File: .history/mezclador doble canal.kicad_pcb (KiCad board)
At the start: 2 copper layers, 166 x 100.5 mm, 17 parts, among them J1 Conn_Coaxial, J2 Conn_Coaxial, J3 Conn_Coaxial, U1 NE5532

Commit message: completè el canal L
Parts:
- removed REF**: Jumper_Wire_10mm, personal:Jumper_Wire_10mm
- JP1: value Jumper_2_Bridged -> Jumper_2_Open; footprint Jumper:SolderJumper-2_P1.3mm_Bridged2Bar_Pad1.0x1.5mm -> personal:Jumper_Wire_10mm
- moved JP1 57.6 mm to (125.0, 77.0), turned to 180 degrees
- moved J2 38.1 mm to (137.7, 85.1), turned to -90 degrees
- moved RV2 31.1 mm to (112.0, 84.5)
- moved RV1 30.2 mm to (126.5, 69.8)
- moved J1 29.7 mm to (137.7, 101.6), turned to -90 degrees
- moved J3 27.8 mm to (108.0, 73.5), turned to 90 degrees
- moved C1 27.2 mm to (124.0, 83.0), turned to 90 degrees
- moved R6 21.4 mm to (118.8, 96.0)
- moved R1 20.8 mm to (128.6, 120.7), turned to 180 degrees
- moved C2 19.0 mm to (108.5, 95.2)
- moved C4 15.9 mm to (137.0, 119.2), turned to 90 degrees
- moved R9 14.4 mm to (128.8, 88.9), turned to 180 degrees
- moved R10 14.0 mm to (118.8, 103.5)
- moved R2 13.2 mm to (113.8, 106.0), turned to 180 degrees
- moved C3 8.28 mm to (125.0, 110.0), turned to -90 degrees
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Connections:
- C1 pad 2: Net-(C1-Pad2) -> Net-(JP1-B)
- JP1 pad 1: unconnected-(JP1-A-Pad1) -> Net-(JP1-A)
- JP1 pad 2: unconnected-(JP1-B-Pad2) -> Net-(JP1-B)
- RV1 pad 2: Net-(C1-Pad2) -> Net-(JP1-A)
- U1 pad 4: unconnected-(U1C-V--Pad4) -> GND
- U1 pad 8: unconnected-(U1C-V+-Pad8) -> VCC
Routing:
- net GND: track 0.00 -> 106.8 mm
- net Net-(U1A--): track 0.00 -> 45.9 mm
- net Net-(C3-Pad2): track 0.00 -> 39.7 mm
- net Net-(U1A-+): track 0.00 -> 25.4 mm
- net Net-(J2-In): track 0.00 -> 20.3 mm
- net Net-(J1-In): track 0.00 -> 18.4 mm
- net VCC: track 0.00 -> 17.2 mm
- net Net-(J3-In): track 0.00 -> 12.7 mm
- net Net-(C2-Pad2): track 0.00 -> 11.3 mm
- net Net-(C2-Pad1): track 0.00 -> 11.0 mm
- net Net-(JP1-A): track 0.00 -> 9.65 mm
- net Net-(C1-Pad1): track 0.00 -> 8.12 mm
- net Net-(JP1-B): track 0.00 -> 5.45 mm
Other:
- board size 166 x 100.5 mm -> 44.5 x 63.5 mm

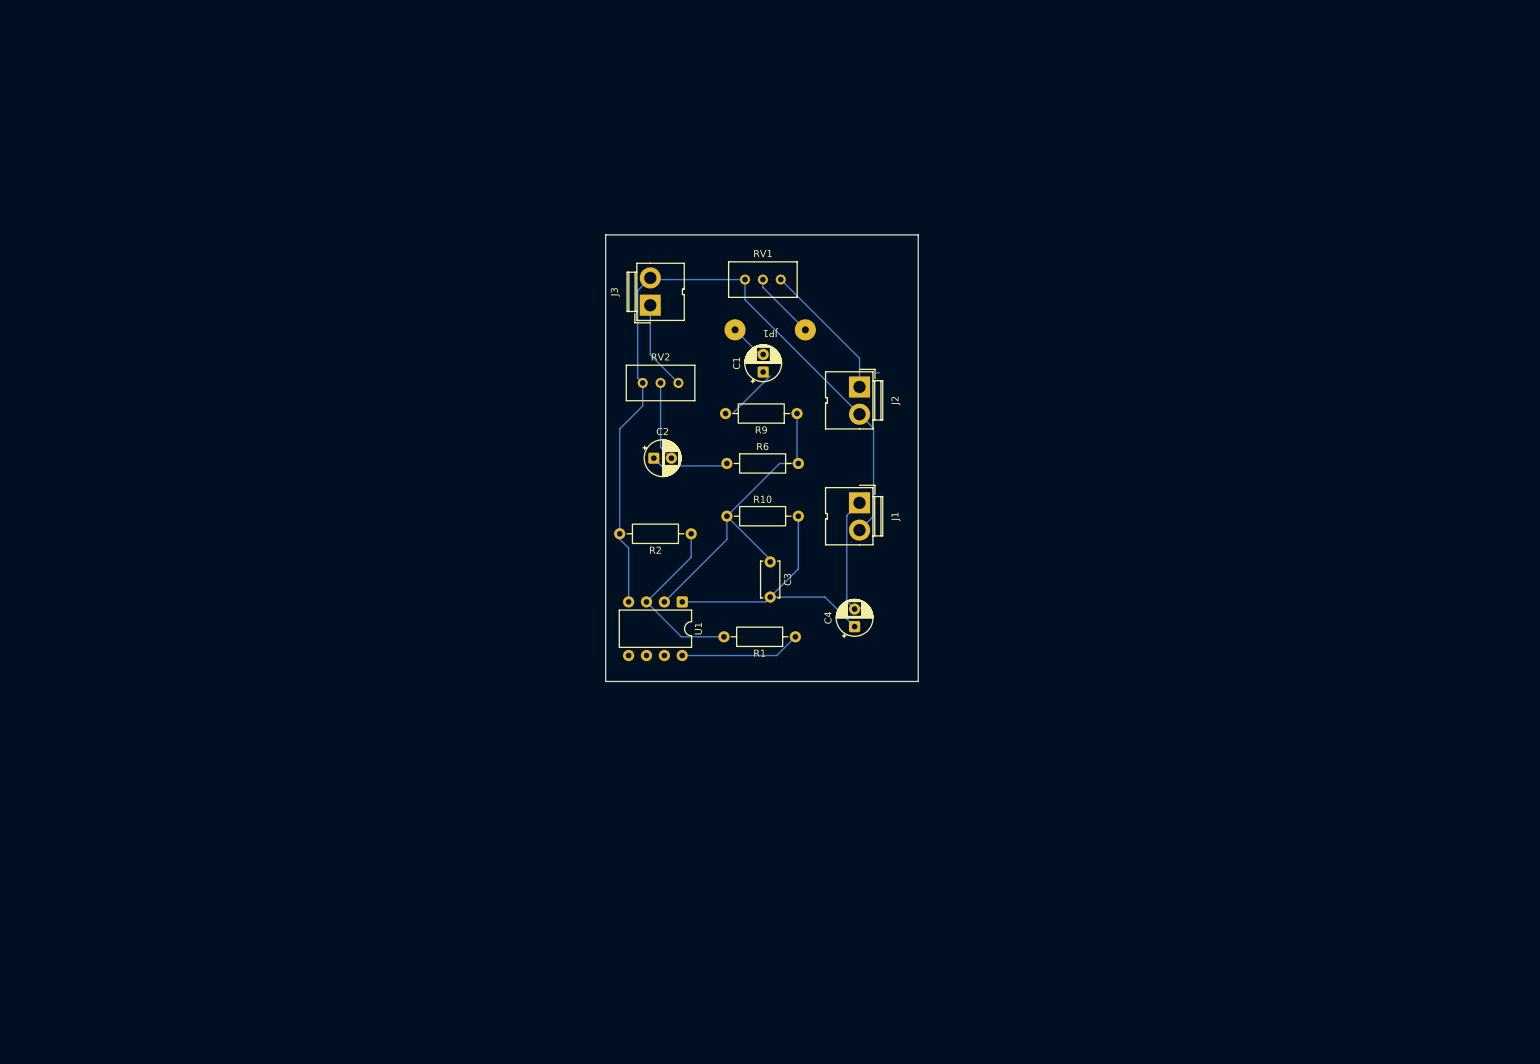
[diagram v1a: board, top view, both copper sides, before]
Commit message: agregando canal r
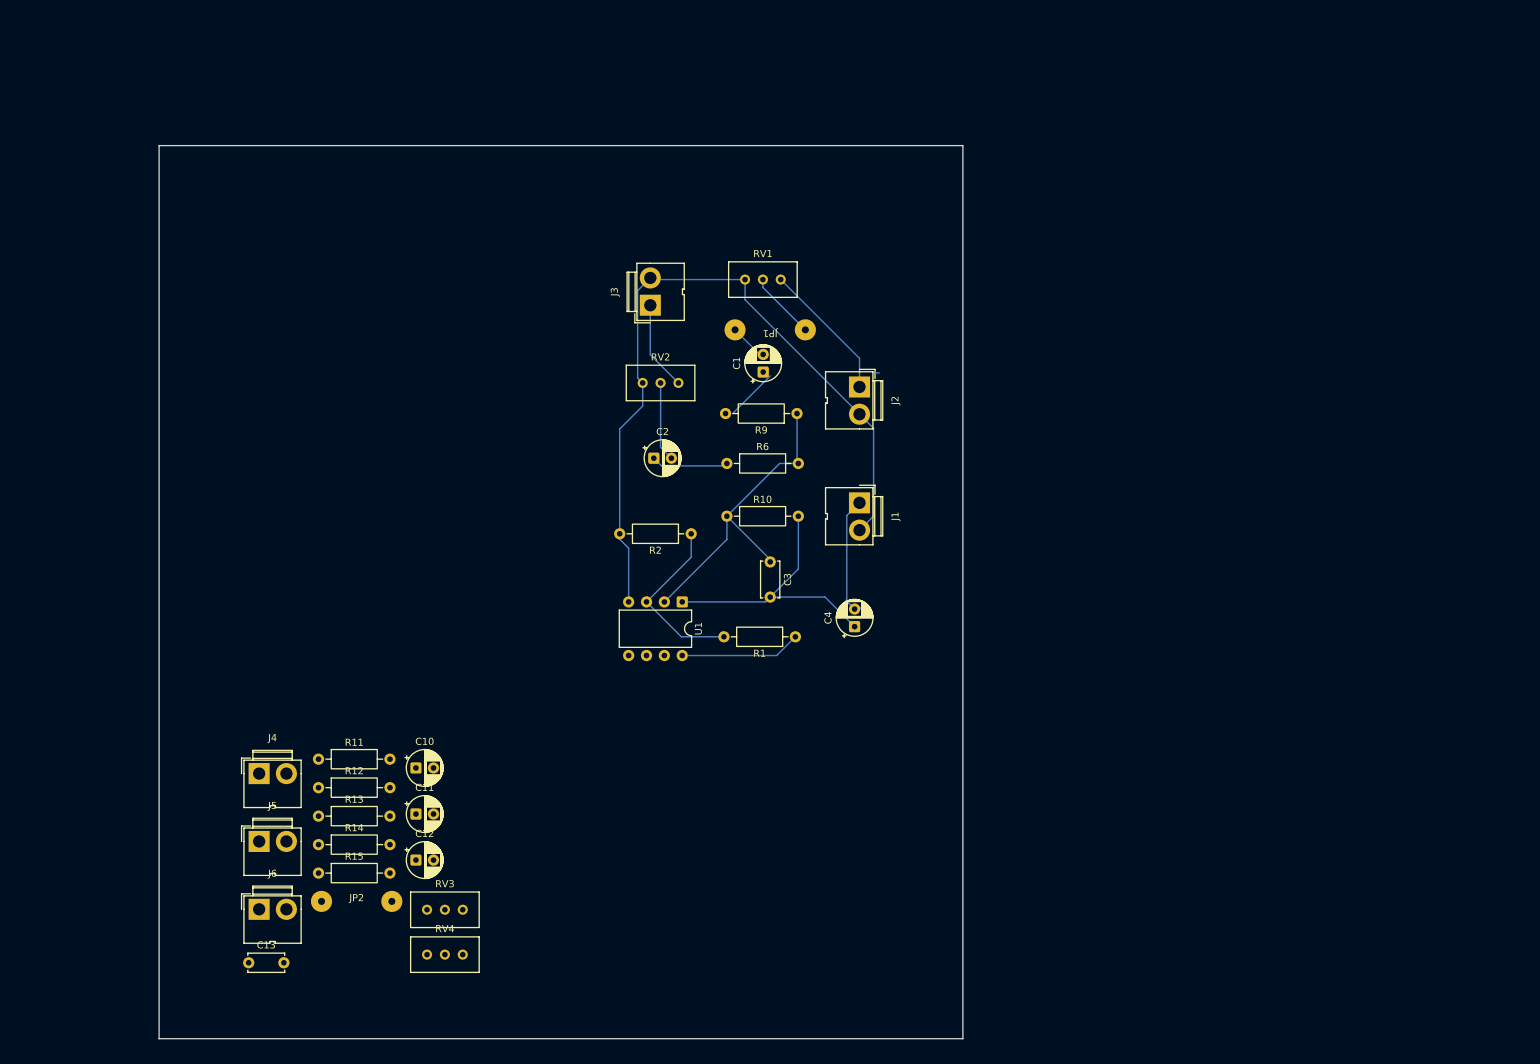
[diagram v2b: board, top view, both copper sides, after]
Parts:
- added C10: C_Polarized_US, Capacitor_THT:CP_Radial_D5.0mm_P2.50mm, F.Cu at (74.6, 139.3)
- added C11: C_Polarized_US, Capacitor_THT:CP_Radial_D5.0mm_P2.50mm, F.Cu at (74.6, 145.8)
- added C12: C_Polarized, Capacitor_THT:CP_Radial_D5.0mm_P2.50mm, F.Cu at (74.6, 152.4)
- added C13: C, Capacitor_THT:C_Disc_D5.0mm_W2.5mm_P5.00mm, F.Cu at (50.8, 167.0)
- added J4: Conn_Coaxial, Connector:JWT_A3963_1x02_P3.96mm_Vertical, F.Cu at (52.3, 140.1)
- added J5: Conn_Coaxial, Connector:JWT_A3963_1x02_P3.96mm_Vertical, F.Cu at (52.3, 149.8)
- added J6: Conn_Coaxial, Connector:JWT_A3963_1x02_P3.96mm_Vertical, F.Cu at (52.3, 159.4)
- added JP2: Jumper_2_Open, personal:Jumper_Wire_10mm, F.Cu at (66.2, 158.3)
- added R11: R, Resistor_THT:R_Axial_DIN0207_L6.3mm_D2.5mm_P10.16mm_Horizontal, F.Cu at (60.8, 138.1)
- added R12: R, Resistor_THT:R_Axial_DIN0207_L6.3mm_D2.5mm_P10.16mm_Horizontal, F.Cu at (60.8, 142.1)
- added R13: R, Resistor_THT:R_Axial_DIN0207_L6.3mm_D2.5mm_P10.16mm_Horizontal, F.Cu at (60.8, 146.2)
- added R14: R, Resistor_THT:R_Axial_DIN0207_L6.3mm_D2.5mm_P10.16mm_Horizontal, F.Cu at (60.8, 150.2)
- added R15: R, Resistor_THT:R_Axial_DIN0207_L6.3mm_D2.5mm_P10.16mm_Horizontal, F.Cu at (60.8, 154.2)
- added RV3: R_Potentiometer, Potentiometer_THT:Potentiometer_Bourns_3296W_Vertical, F.Cu at (81.3, 159.5)
- added RV4: R_Potentiometer, Potentiometer_THT:Potentiometer_Bourns_3296W_Vertical, F.Cu at (81.3, 165.8)
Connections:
- RV2 pad 1: Net-(J3-In) -> GND
- RV2 pad 3: GND -> Net-(J3-In)
- U1 pad 5: unconnected-(U1B-+-Pad5) -> Net-(U1B-+)
- U1 pad 6: unconnected-(U1B---Pad6) -> Net-(U1B--)
- U1 pad 7: unconnected-(U1-Pad7) -> Net-(C12-Pad1)
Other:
- board size 44.5 x 63.5 mm -> 114.3 x 127 mm

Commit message: separando componentes
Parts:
- moved J4 38.5 mm to (50.8, 101.6)
- moved R11 29.8 mm to (78.7, 114.3)
- moved J5 22.8 mm to (50.8, 127.0)
- moved RV3 21.5 mm to (101.6, 152.4)
- moved RV4 20.3 mm to (101.6, 165.1)
- moved C10 17.0 mm to (86.4, 127.0)
- moved J6 7.16 mm to (50.8, 152.4)
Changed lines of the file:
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@@
 	(footprint "Potentiometer_THT:Potentiometer_Bourns_3296W_Vertical"
 		(layer "F.Cu")
-		(at 81.28 159.46)
+		(at 101.6 152.4)
 		(descr "Potentiometer, vertical, Bourns 3296W, https://www.bourns.com/pdfs/3296.pdf")
 		(tags "Potentiometer vertical Bourns 3296W")
@@
 	(footprint "Potentiometer_THT:Potentiometer_Bourns_3296W_Vertical"
 		(layer "F.Cu")
-		(at 81.28 165.84)
+		(at 101.6 165.1)
 		(descr "Potentiometer, vertical, Bourns 3296W, https://www.bourns.com/pdfs/3296.pdf")
 		(tags "Potentiometer vertical Bourns 3296W")
@@
 	(footprint "Resistor_THT:R_Axial_DIN0207_L6.3mm_D2.5mm_P10.16mm_Horizontal"
 		(layer "F.Cu")
-		(at 60.77 138.05)
+		(at 78.74 114.3)
 		(descr "Resistor, Axial_DIN0207 series, Axial, Horizontal, pin pitch=10.16mm, 0.25W = 1/4W, length*diameter=6.3*2.5mm^2, http://cdn-reichelt.de/documents/datenblatt/B400/1_4W%23YAG.pdf")
 		(tags "Resistor Axial_DIN0207 series Axial Horizontal pin pitch 10.16mm 0.25W = 1/4W length 6.3mm diameter 2.5mm")
@@
 	(footprint "Connector:JWT_A3963_1x02_P3.96mm_Vertical"
 		(layer "F.Cu")
-		(at 52.325 159.4)
+		(at 50.8 152.4)
 		(descr "JWT A3963, 3.96mm pitch Pin head connector (http://www.jwt.com.tw/pro_pdf/A3963.pdf)")
 		(tags "connector JWT A3963 pinhead")
@@
 	(footprint "Connector:JWT_A3963_1x02_P3.96mm_Vertical"
 		(layer "F.Cu")
-		(at 52.325 140.1)
+		(at 50.8 101.6)
 		(descr "JWT A3963, 3.96mm pitch Pin head connector (http://www.jwt.com.tw/pro_pdf/A3963.pdf)")
 		(tags "connector JWT A3963 pinhead")
@@
 	(footprint "Capacitor_THT:CP_Radial_D5.0mm_P2.50mm"
 		(layer "F.Cu")
-		(at 74.619775 139.3)
+		(at 86.4 127)
 		(descr "CP, Radial series, Radial, pin pitch=2.50mm, diameter=5mm, height=7mm, Electrolytic Capacitor")
 		(tags "CP Radial series Radial pin pitch 2.50mm diameter 5mm height 7mm Electrolytic Capacitor")
@@
 	(footprint "Connector:JWT_A3963_1x02_P3.96mm_Vertical"
 		(layer "F.Cu")
-		(at 52.325 149.75)
+		(at 50.8 127)
 		(descr "JWT A3963, 3.96mm pitch Pin head connector (http://www.jwt.com.tw/pro_pdf/A3963.pdf)")
 		(tags "connector JWT A3963 pinhead")
@@
 	)
 	(segment
-		(start 123.96 70.96)
-		(end 130 77)
+		(start 103.6 106.78)
+		(end 104.87 108.05)
 		(width 0.2)
 		(layer "B.Cu")
-		(net "Net-(JP1-A)")
+		(net "GND")
 	)
 	(segment
-		(start 123.96 69.85)
-		(end 123.96 70.96)
+		(start 106.150001 83.830001)
+		(end 106.87 84.55)
 		(width 0.2)
 		(layer "B.Cu")
-		(net "Net-(JP1-A)")
+		(net "GND")
 	)
 	(segment
-		(start 123.5 80.5)
-		(end 124 80.5)
+		(start 121.42 72.72)
+		(end 137.7 89)
 		(width 0.2)
 		(layer "B.Cu")
-		(net "Net-(JP1-B)")
+		(net "GND")
 	)
 	(segment
-		(start 120 77)
-		(end 123.5 80.5)
+		(start 121.42 69.85)
+		(end 121.42 72.72)
 		(width 0.2)
 		(layer "B.Cu")
-		(net "Net-(JP1-B)")
+		(net "GND")
 	)
 	(segment
-		(start 129 111)
-		(end 125 115)
+		(start 106.87 87.82)
+		(end 103.6 91.09)
 		(width 0.2)
 		(layer "B.Cu")
-		(net "Net-(C3-Pad2)")
+		(net "GND")
 	)
 	(segment
-		(start 112.49 115.69)
-		(end 124.31 115.69)
+		(start 107.95 69.62)
+		(end 108.18 69.85)
 		(width 0.2)
 		(layer "B.Cu")
-		(net "Net-(C3-Pad2)")
+		(net "GND")
 	)
 	(segment
-		(start 129 103.5)
-		(end 129 111)
+		(start 104.87 108.05)
+		(end 104.87 115.69)
 		(width 0.2)
 		(layer "B.Cu")
-		(net "Net-(C3-Pad2)")
+		(net "GND")
 	)
 	(segment
-		(start 125 115)
-		(end 132.794887 115)
+		(start 137.7 89)
+		(end 139.7 91)
 		(width 0.2)
 		(layer "B.Cu")
-		(net "Net-(C3-Pad2)")
+		(net "GND")
 	)
 	(segment
-		(start 132.794887 115)
-		(end 137 119.205113)
+		(start 139.7 103.48)
+		(end 137.7 105.48)
 		(width 0.2)
 		(layer "B.Cu")
-		(net "Net-(C3-Pad2)")
+		(net "GND")
 	)
 	(segment
-		(start 124.31 115.69)
-		(end 125 115)
+		(start 106.15 71.42)
+		(end 106.150001 83.830001)
 		(width 0.2)
 		(layer "B.Cu")
-		(net "Net-(C3-Pad2)")
+		(net "GND")
 	)
 	(segment
-		(start 135.9 115.605113)
-		(end 137 116.705113)
+		(start 106.87 84.55)
+		(end 106.87 87.82)
 		(width 0.2)
 		(layer "B.Cu")
-		(net "Net-(J1-In)")
+		(net "GND")
 	)
 	(segment
-		(start 137.75 116.455113)
-		(end 138 116.705113)
+		(start 121.3 69.62)
+		(end 121.42 69.5)
 		(width 0.2)
 		(layer "B.Cu")
-		(net "Net-(J1-In)")
+		(net "GND")
 	)
 	(segment
-		(start 135.9 103.4)
-		(end 135.9 115.605113)
+		(start 108.18 69.85)
+		(end 121.42 69.85)
 		(width 0.2)
 		(layer "B.Cu")
-		(net "Net-(J1-In)")
+		(net "GND")
 	)
 	(segment
-		(start 135.75 115.455113)
-		(end 137 116.705113)
+		(start 103.6 91.09)
+		(end 103.6 106)
 		(width 0.2)
 		(layer "B.Cu")
-		(net "Net-(J1-In)")
+		(net "GND")
 	)
 	(segment
-		(start 137.7 101.6)
-		(end 135.9 103.4)
+		(start 103.6 106)
+		(end 103.6 106.78)
 		(width 0.2)
 		(layer "B.Cu")
-		(net "Net-(J1-In)")
+		(net "GND")
 	)
 	(segment
-		(start 126.5 69.85)
-		(end 137.7 81.05)
+		(start 139.7 91)
+		(end 139.7 103.48)
 		(width 0.2)
 		(layer "B.Cu")
-		(net "Net-(J2-In)")
+		(net "GND")
 	)
 	(segment
-		(start 140.12 83.12)
-		(end 140.5 83.12)
+		(start 107.95 69.62)
+		(end 106.15 71.42)
 		(width 0.2)
 		(layer "B.Cu")
-		(net "Net-(J2-In)")
+		(net "GND")
 	)
 	(segment
-		(start 137.7 81.05)
-		(end 137.7 85.12)
+		(start 123.96 70.96)
+		(end 130 77)
 		(width 0.2)
 		(layer "B.Cu")
-		(net "Net-(J2-In)")
+		(net "Net-(JP1-A)")
 	)
 	(segment
-		(start 103.6 106.78)
-		(end 104.87 108.05)
+		(start 123.96 69.85)
+		(end 123.96 70.96)
 		(width 0.2)
 		(layer "B.Cu")
-		(net "GND")
+		(net "Net-(JP1-A)")
 	)
 	(segment
-		(start 106.150001 83.830001)
-		(end 106.87 84.55)
+		(start 123.5 80.5)
+		(end 124 80.5)
 		(width 0.2)
 		(layer "B.Cu")
-		(net "GND")
+		(net "Net-(JP1-B)")
 	)
 	(segment
-		(start 121.42 72.72)
-		(end 137.7 89)
+		(start 120 77)
+		(end 123.5 80.5)
 		(width 0.2)
 		(layer "B.Cu")
-		(net "GND")
+		(net "Net-(JP1-B)")
 	)
 	(segment
-		(start 121.42 69.85)
-		(end 121.42 72.72)
+		(start 129 111)
+		(end 125 115)
 		(width 0.2)
 		(layer "B.Cu")
-		(net "GND")
+		(net "Net-(C3-Pad2)")
 	)
 	(segment
-		(start 106.87 87.82)
-		(end 103.6 91.09)
+		(start 112.49 115.69)
+		(end 124.31 115.69)
 		(width 0.2)
 		(layer "B.Cu")
-		(net "GND")
+		(net "Net-(C3-Pad2)")
 	)
 	(segment
-		(start 107.95 69.62)
-		(end 108.18 69.85)
+		(start 129 103.5)
+		(end 129 111)
 		(width 0.2)
 		(layer "B.Cu")
-		(net "GND")
+		(net "Net-(C3-Pad2)")
 	)
 	(segment
-		(start 104.87 108.05)
-		(end 104.87 115.69)
+		(start 125 115)
+		(end 132.794887 115)
 		(width 0.2)
 		(layer "B.Cu")
-		(net "GND")
+		(net "Net-(C3-Pad2)")
 	)
 	(segment
-		(start 137.7 89)
-		(end 139.7 91)
+		(start 132.794887 115)
+		(end 137 119.205113)
 		(width 0.2)
 		(layer "B.Cu")
-		(net "GND")
+		(net "Net-(C3-Pad2)")
 	)
 	(segment
-		(start 139.7 103.48)
-		(end 137.7 105.48)
+		(start 124.31 115.69)
+		(end 125 115)
 		(width 0.2)
 		(layer "B.Cu")
-		(net "GND")
+		(net "Net-(C3-Pad2)")
 	)
 	(segment
-		(start 106.15 71.42)
-		(end 106.150001 83.830001)
+		(start 135.9 115.605113)
+		(end 137 116.705113)
 		(width 0.2)
 		(layer "B.Cu")
-		(net "GND")
+		(net "Net-(J1-In)")
 	)
 	(segment
-		(start 106.87 84.55)
-		(end 106.87 87.82)
+		(start 137.75 116.455113)
+		(end 138 116.705113)
 		(width 0.2)
 		(layer "B.Cu")
-		(net "GND")
+		(net "Net-(J1-In)")
 	)
 	(segment
-		(start 121.3 69.62)
-		(end 121.42 69.5)
+		(start 135.9 103.4)
+		(end 135.9 115.605113)
 		(width 0.2)
 		(layer "B.Cu")
-		(net "GND")
+		(net "Net-(J1-In)")
 	)
 	(segment
-		(start 108.18 69.85)
-		(end 121.42 69.85)
+		(start 135.75 115.455113)
+		(end 137 116.705113)
 		(width 0.2)
 		(layer "B.Cu")
-		(net "GND")
+		(net "Net-(J1-In)")
 	)
 	(segment
-		(start 103.6 91.09)
-		(end 103.6 106)
+		(start 137.7 101.6)
+		(end 135.9 103.4)
 		(width 0.2)
 		(layer "B.Cu")
-		(net "GND")
+		(net "Net-(J1-In)")
 	)
 	(segment
-		(start 103.6 106)
-		(end 103.6 106.78)
+		(start 125.92 123.31)
+		(end 112.49 123.31)
 		(width 0.2)
 		(layer "B.Cu")
-		(net "GND")
+		(net "VCC")
 	)
 	(segment
-		(start 139.7 91)
-		(end 139.7 103.48)
+		(start 128.58 120.65)
+		(end 125.92 123.31)
 		(width 0.2)
 		(layer "B.Cu")
-		(net "GND")
+		(net "VCC")
 	)
 	(segment
-		(start 107.95 69.62)
-		(end 106.15 71.42)
+		(start 126.5 69.85)
+		(end 137.7 81.05)
 		(width 0.2)
 		(layer "B.Cu")
-		(net "GND")
+		(net "Net-(J2-In)")
+	)
+	(segment
+		(start 140.12 83.12)
+		(end 140.5 83.12)
+		(width 0.2)
+		(layer "B.Cu")
+		(net "Net-(J2-In)")
+	)
+	(segment
+		(start 137.7 81.05)
+		(end 137.7 85.12)
+		(width 0.2)
+		(layer "B.Cu")
+		(net "Net-(J2-In)")
 	)
 	(segment
@@
 	)
 	(segment
-		(start 125.92 123.31)
-		(end 112.49 123.31)
-		(width 0.2)
-		(layer "B.Cu")
-		(net "VCC")
-	)
-	(segment
-		(start 128.58 120.65)
-		(end 125.92 123.31)
-		(width 0.2)
-		(layer "B.Cu")
-		(net "VCC")
-	)
-	(segment

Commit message: trabajando canal R
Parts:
- removed JP2: Jumper_2_Open, personal:Jumper_Wire_10mm
- added J7: Screw_Terminal_01x02, Connector:JWT_A3963_1x02_P3.96mm_Vertical, F.Cu at (177.8, 40.8)
- moved J5 161.0 mm to (186.8, 40.8), turned to 90 degrees
- moved C13 158.3 mm to (195.2, 102.0)
- moved R14 152.2 mm to (203.2, 96.6), turned to 180 degrees
- moved R15 140.3 mm to (193.0, 107.4)
- moved R11 114.6 mm to (186.8, 76.2), turned to 90 degrees
- moved J1 93.8 mm to (225.8, 69.3)
- moved J2 93.8 mm to (225.8, 52.8)
- moved C2 93.8 mm to (196.6, 62.9)
- moved J3 93.8 mm to (196.1, 41.2)
- moved R2 93.8 mm to (201.9, 73.7)
- moved RV2 93.8 mm to (200.1, 52.2)
- moved U1 93.8 mm to (200.6, 83.4)
- moved C1 93.8 mm to (212.1, 50.7)
- moved C3 93.8 mm to (213.1, 77.7)
- moved C4 93.8 mm to (225.1, 86.9)
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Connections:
- C10 pad 2: Net-(JP2-B) -> Net-(C10-Pad2)
- RV3 pad 2: Net-(JP2-A) -> Net-(C10-Pad2)
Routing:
- net GND: track 106.8 -> 125.2 mm
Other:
- board size 114.3 x 127 mm -> 60.4 x 124 mm
- board text added: "nestorotero@abc.gob.ar"

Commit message: reduciendo espacio desperdiciado
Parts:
- moved C12 182.8 mm to (188.2, 99.6)
- moved C11 153.7 mm to (177.1, 68.5), turned to -90 degrees
- moved J4 140.7 mm to (177.8, 102.5), turned to 90 degrees
- moved R13 140.2 mm to (176.6, 65.0), turned to 90 degrees
- moved J6 119.8 mm to (179.4, 86.9), turned to -90 degrees
- moved R12 117.8 mm to (183.1, 62.7), turned to -90 degrees
- moved RV4 114.0 mm to (181.6, 77.2), turned to 0 degrees
- moved C10 105.3 mm to (181.7, 56.8)
- moved RV3 92.7 mm to (189.4, 58.5), turned to 180 degrees
- moved RV2 15.5 mm to (193.9, 66.5), turned to 180 degrees
- moved C1 11.5 mm to (211.9, 62.2)
- moved JP1 10.4 mm to (211.8, 55.0)
- moved R9 10.4 mm to (216.7, 67.0)
- moved C2 10.2 mm to (198.0, 73.0), turned to 180 degrees
- moved J7 9.79 mm to (176.5, 50.5)
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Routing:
- net VCC: track 17.2 -> 131.6 mm
- net Net-(U1B--): track 0.00 -> 33.8 mm
- net Net-(C12-Pad1): track 0.00 -> 29.6 mm
- net Net-(U1B-+): track 0.00 -> 13.8 mm
- net Net-(J4-In): track 0.00 -> 12.6 mm
- net Net-(J6-In): track 0.00 -> 10.9 mm
- net Net-(C10-Pad2): track 0.00 -> 9.30 mm
- net Net-(J5-In): track 0.00 -> 9.00 mm
- net Net-(C11-Pad2): track 0.00 -> 6.98 mm
- net Net-(C10-Pad1): track 0.00 -> 6.47 mm
- net Net-(U1A--): track 45.9 -> 39.5 mm
- net Net-(J1-In): track 18.4 -> 13.3 mm
- net Net-(C2-Pad2): track 11.3 -> 6.90 mm
- net Net-(J3-In): track 12.7 -> 17.0 mm
- net Net-(U1A-+): track 25.4 -> 21.2 mm
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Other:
- board size 60.4 x 124 mm -> 56.7 x 63.9 mm

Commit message: acomodando componentes
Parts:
- moved C4 16.8 mm to (222.2, 70.3)
- moved R1 15.5 mm to (225.6, 75.7)
- moved J2 14.3 mm to (223.7, 47.8)
- moved J1 13.5 mm to (224.5, 61.5)
- moved C3 6.56 mm to (206.5, 75.8), turned to 0 degrees
- moved R6 5.07 mm to (206.4, 66.5)
- moved R10 4.94 mm to (206.5, 71.4)
- moved R9 4.62 mm to (216.5, 62.3)
- moved C1 4.00 mm to (211.9, 58.2)
- moved JP1 2.00 mm to (211.8, 53.0)
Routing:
- net GND: track 125.4 -> 177.4 mm
- net VCC: track 131.6 -> 92.9 mm
- net Net-(U1B--): track 33.8 -> 57.0 mm
- net Net-(U1A-+): track 21.2 -> 32.2 mm
- net Net-(J2-In): track 19.4 -> 10.0 mm
- net Net-(C3-Pad2): track 36.8 -> 27.5 mm
- net Net-(J1-In): track 13.3 -> 7.28 mm
- net Net-(JP1-A): track 10.2 -> 8.16 mm
- net Net-(C2-Pad1): track 9.34 -> 11.1 mm
- net Net-(U1A--): track 39.5 -> 40.6 mm
- net Net-(JP1-B): track 7.04 -> 6.21 mm
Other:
- board size 56.7 x 63.9 mm -> 54.4 x 61.3 mm
